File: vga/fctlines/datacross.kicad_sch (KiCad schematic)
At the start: 8 parts, among them U1 74AHC541, U10 74AHC541, U2 74AHC541, U5 74HC245, U6 74HC245, U7 74AHC541, U8 74HC245, U9 74HC245

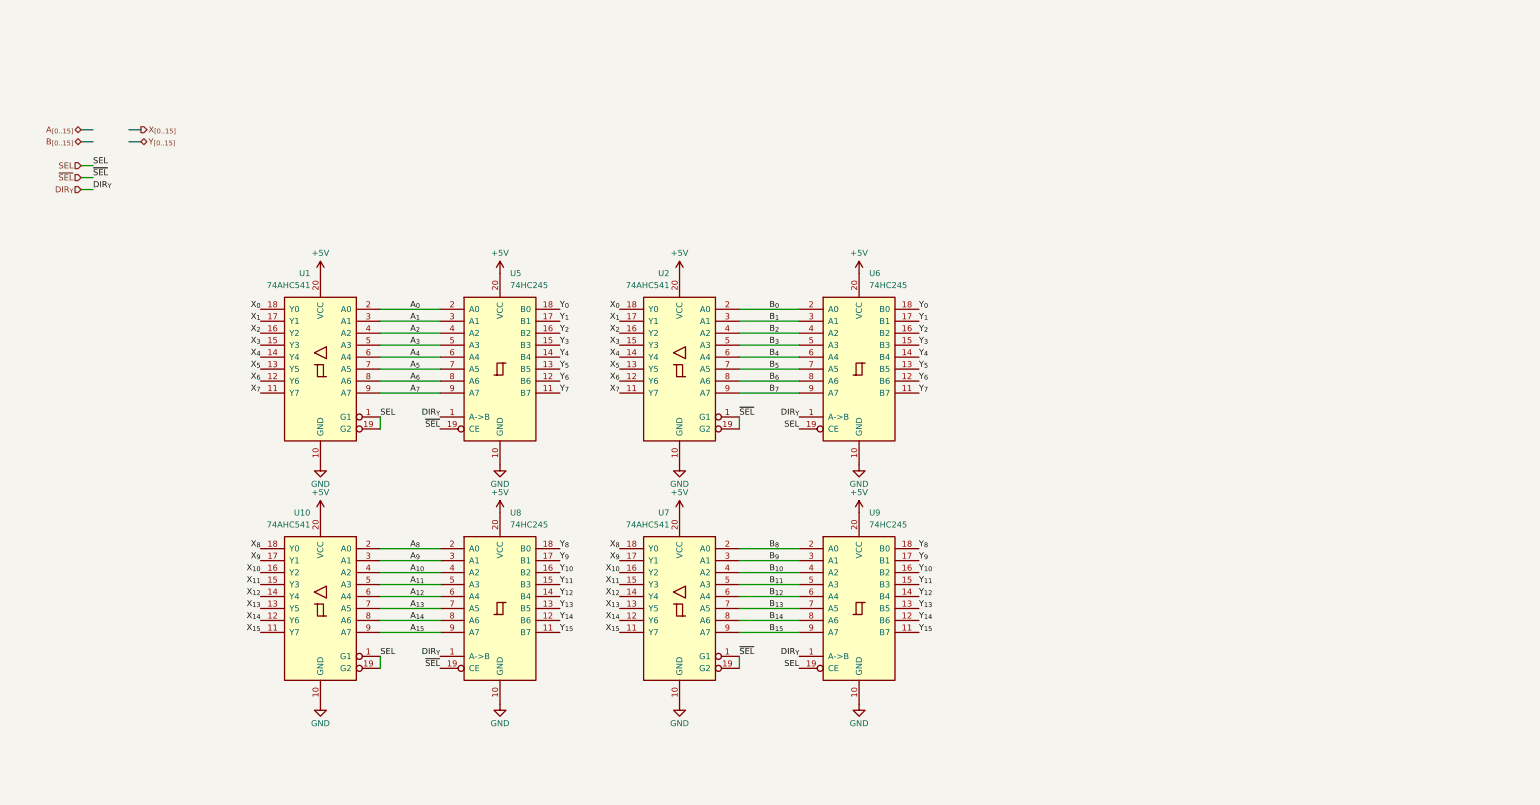
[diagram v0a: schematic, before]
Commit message: [vga/fctlines] corrected errors on schematic. Schematic & PCB are NO longer matching.
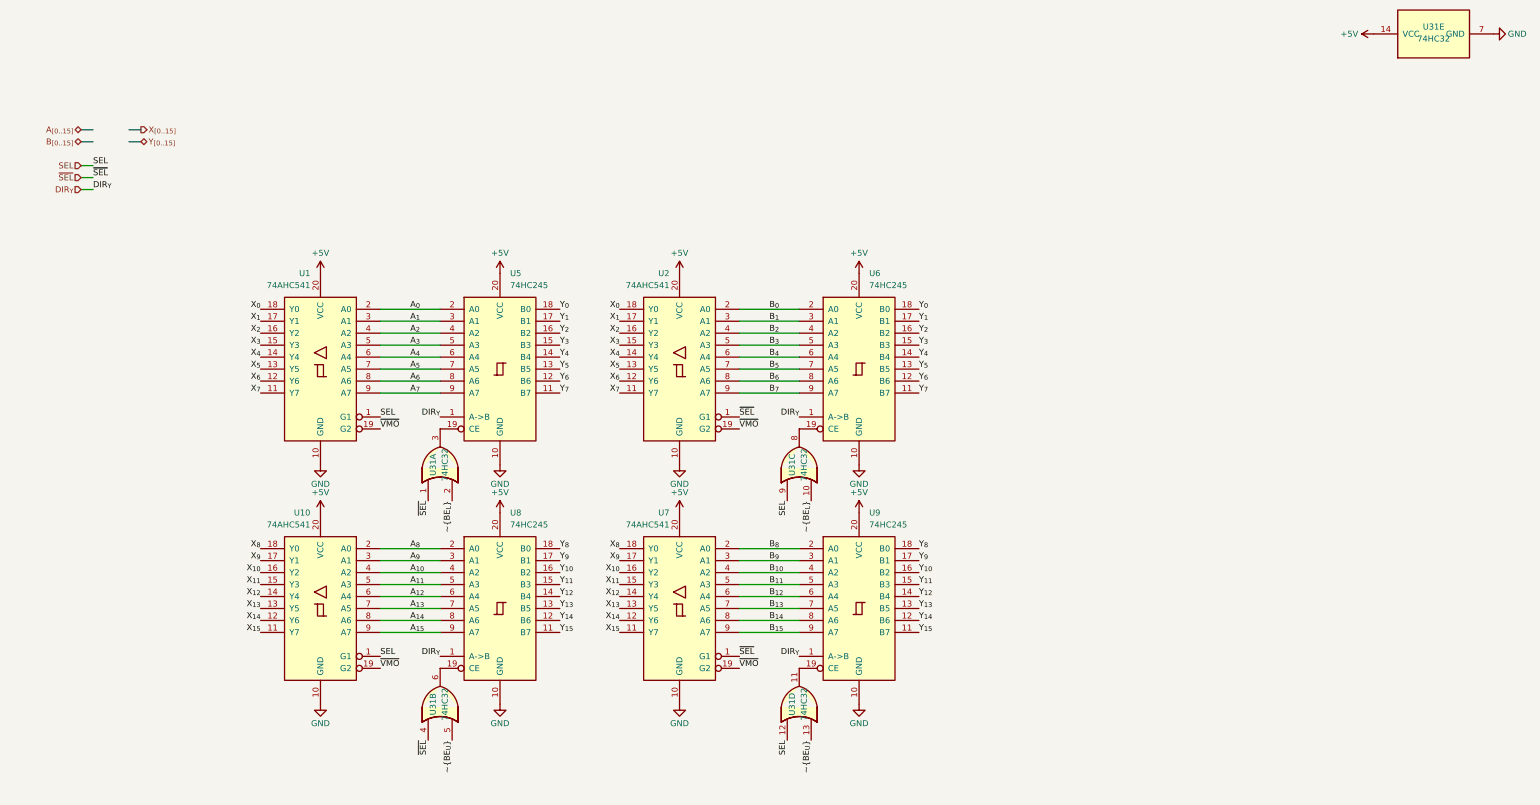
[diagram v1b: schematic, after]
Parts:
- added U31: 74HC32, symbol 74xx:74LS32
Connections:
- net +5V: now also U31.14 (VCC)
- net GND: now also U31.7 (GND)
- net SEL: now also U31.12, U31.9; no longer U1.19 (G2), U10.19 (G2), U6.19 (CE), U9.19 (CE)
- net ~{SEL}: now also U31.1, U31.4; no longer U2.19 (G2), U5.19 (CE), U7.19 (G2), U8.19 (CE)
- new net: U31.8, U6.19 (CE)
- new net: U31.6, U8.19 (CE)
- new net: U31.3, U5.19 (CE)
- new net: U31.11, U9.19 (CE)
- new net ~{BE_{L}}: U31.10, U31.2
- new net ~{BE_{U}}: U31.13, U31.5
- new net ~{VMO}: U1.19 (G2), U10.19 (G2), U2.19 (G2), U7.19 (G2)
